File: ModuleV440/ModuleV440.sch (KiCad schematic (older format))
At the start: 49 parts, among them J2 AVR-ISP-6, Q1 AO3400A, U1 EL3H7(B)(TA)-G, Y1 8MHZ Ceramic Resonator

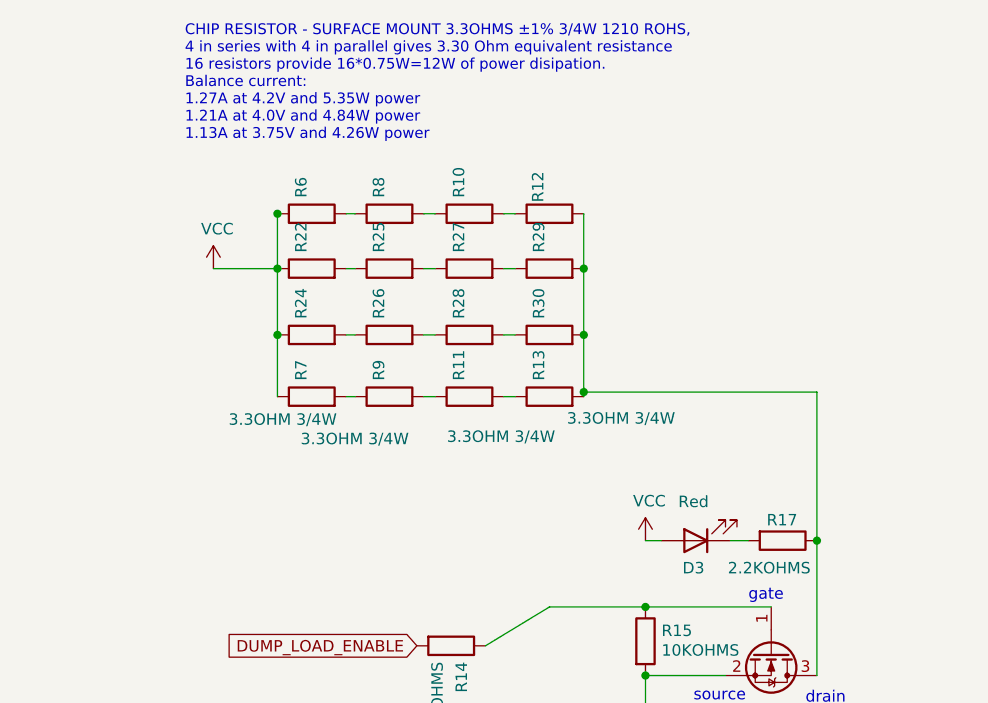
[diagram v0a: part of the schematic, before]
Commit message: Change resistor physical size to upgrade to 3/4W power rating
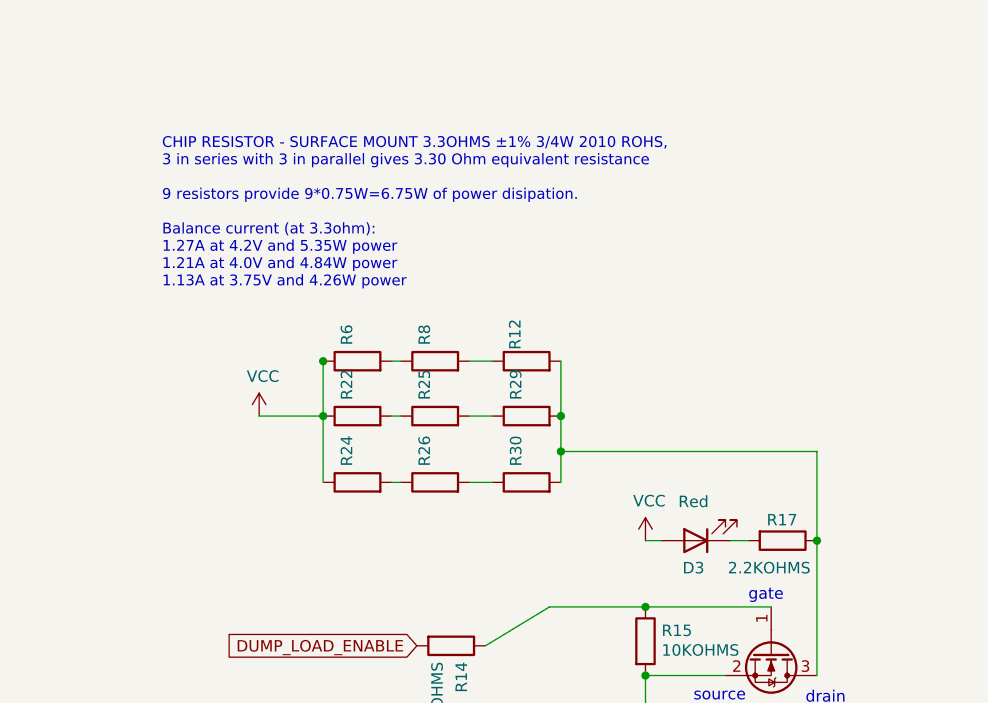
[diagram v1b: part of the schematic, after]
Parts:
- removed R10, R11, R13, R27, R28, R7, R9: 3.3OHM 3/4W, Resistor_SMD:R_1210_3225Metric, symbol Device:R
- R12, R22, R24, R25, R26, R29, R30, R6, R8: footprint Resistor_SMD:R_1210_3225Metric -> Resistor_SMD:R_2010_5025Metric; JLCPCBRotation 0 -> (none); LCSCStockCode C21624 -> C270971; PartNumber 1210W3F330KT5E -> 201007F330KT4E
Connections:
- wire segments 139 -> 131
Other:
- note added: "CHIP RESISTOR - SURFACE MOUNT 3.3OHMS ±1% 3/4W 2010 ROHS, \n3 in series with 3 in parallel gives 3.30 Ohm equivalent resistance\n\n9 resistors provide 9*0.75W=6.75W of power disipation.\n\nBalance current (at 3.3ohm):\n1.27A at 4.2V and 5.35W power\n1.21A at 4.0V and 4.84W power\n1.13A at 3.75V and 4.26W power\n\n\n"
- note removed: "CHIP RESISTOR - SURFACE MOUNT 3.3OHMS ±1% 3/4W 1210 ROHS, \n4 in series with 4 in parallel gives 3.30 Ohm equivalent resistance\n16 resistors provide 16*0.75W=12W of power disipation.\nBalance current:\n1.27A at 4.2V and 5.35W power\n1.21A at 4.0V and 4.84W power\n1.13A at 3.75V and 4.26W power\n\n\n"
- moved on the sheet: R12, R22, R24, R25, R26, R29, R30, R6, R8

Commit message: Update ModuleV440.sch
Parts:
- D2: JLCPCBRotation (none) -> 0
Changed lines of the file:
@@
 F 3 "https://datasheet.lcsc.com/szlcsc/1912111437_AnBon-SMBJ5-0A_C440263.pdf" H 5725 7025 50  0001 C CNN
 F 4 "C440263" V 5725 7025 50  0001 C CNN "LCSCStockCode"
-F 5 "" V 5725 7025 50  0001 C CNN "JLCPCBRotation"
+F 5 "0" V 5725 7025 50  0001 C CNN "JLCPCBRotation"
 	1    5725 7025
 	0    -1   -1   0

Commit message: Update R14 510ohm resistor part number (JLCPCB) (#80)
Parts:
- R14: LCSCStockCode C17734 -> C25317; PartNumber 0805W8F5100T5E -> 0805W8J0511T5E
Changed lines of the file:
@@
 F 2 "Resistor_SMD:R_0805_2012Metric" V 8845 3375 50  0001 C CNN
 F 3 "" H 8915 3375 50  0001 C CNN
-F 4 "C17734" V 4095 4915 50  0001 C CNN "LCSCStockCode"
-F 5 "0805W8F5100T5E" V 4095 4915 50  0001 C CNN "PartNumber"
+F 4 "C25317" V 4095 4915 50  0001 C CNN "LCSCStockCode"
+F 5 "0805W8J0511T5E" V 4095 4915 50  0001 C CNN "PartNumber"
 	1    8915 3375
 	0    1    1    0

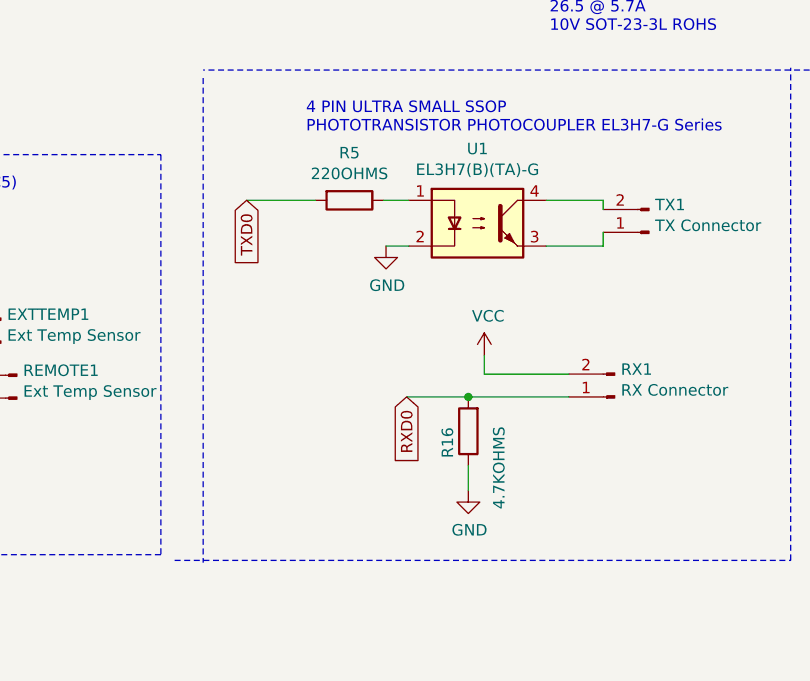
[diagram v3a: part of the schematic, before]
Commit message: Changes R16 to 2.2K to match controller board
Changed part on R14 to basic JLCPCB part rather than extended
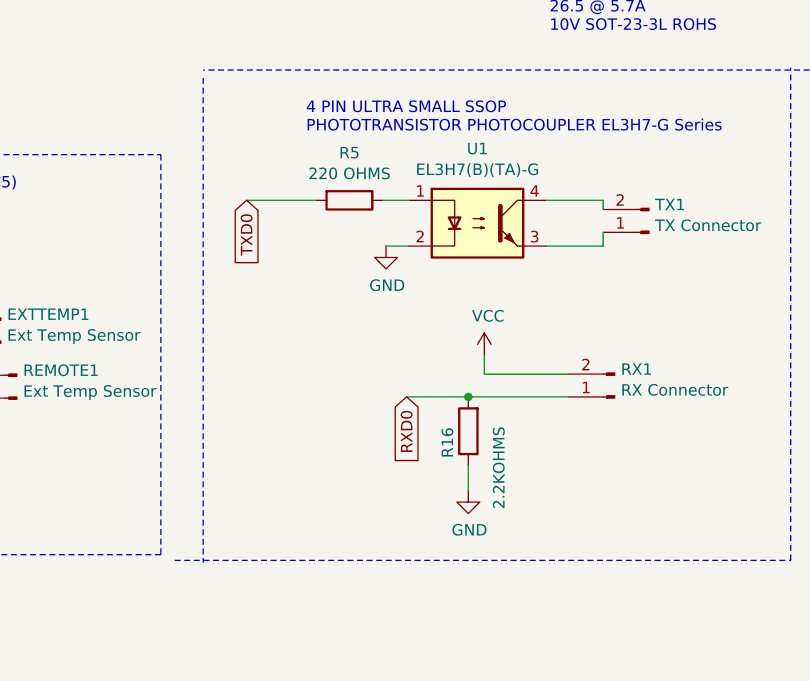
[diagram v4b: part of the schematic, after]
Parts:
- R14: LCSCStockCode C25317 -> C17734; PartNumber 0805W8J0511T5E -> 0805W8F5100T5E
- R16: value 4.7KOHMS -> 2.2KOHMS; JLCPCBRotation 0 -> (none); LCSCStockCode C17673 -> C17520; PartNumber 0805W8F4701T5E -> 0805W8F2201T5E
- R5: value 220OHMS -> 220 OHMS
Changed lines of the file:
@@
 P 9080 4860
 F 0 "R5" V 8873 4860 50  0000 C CNN
-F 1 "220OHMS" V 8964 4860 50  0000 C CNN
+F 1 "220 OHMS" V 8964 4860 50  0000 C CNN
 F 2 "Resistor_SMD:R_0805_2012Metric" V 9010 4860 50  0001 C CNN
 F 3 "" H 9080 4860 50  0001 C CNN
@@
 P 9600 5870
 F 0 "R16" V 9690 5920 50  0000 C CNN
-F 1 "4.7KOHMS" V 9465 6030 50  0000 C CNN
+F 1 "2.2KOHMS" V 9465 6030 50  0000 C CNN
 F 2 "Resistor_SMD:R_0805_2012Metric" V 9530 5870 50  0001 C CNN
 F 3 "" H 9600 5870 50  0001 C CNN
-F 4 "C17673" V 3570 5040 50  0001 C CNN "LCSCStockCode"
-F 5 "0805W8F4701T5E" V 3570 5040 50  0001 C CNN "PartNumber"
-F 6 "0" V 9600 5870 50  0001 C CNN "JLCPCBRotation"
+F 4 "C17520" V 3570 5040 50  0001 C CNN "LCSCStockCode"
+F 5 "0805W8F2201T5E" V 3570 5040 50  0001 C CNN "PartNumber"
 	1    9600 5870
 	-1   0    0    1
@@
 F 2 "Resistor_SMD:R_0805_2012Metric" V 8845 3375 50  0001 C CNN
 F 3 "" H 8915 3375 50  0001 C CNN
-F 4 "C25317" V 4095 4915 50  0001 C CNN "LCSCStockCode"
-F 5 "0805W8J0511T5E" V 4095 4915 50  0001 C CNN "PartNumber"
+F 4 "C17734" V 4095 4915 50  0001 C CNN "LCSCStockCode"
+F 5 "0805W8F5100T5E" V 4095 4915 50  0001 C CNN "PartNumber"
 	1    8915 3375
 	0    1    1    0
